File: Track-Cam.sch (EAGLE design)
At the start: 38 parts, among them IC1 STM32F042KT/M, IC2 BD6211F/M, IC3 BD6211F/M, X1 RASPI_BOARD_B+#_HC

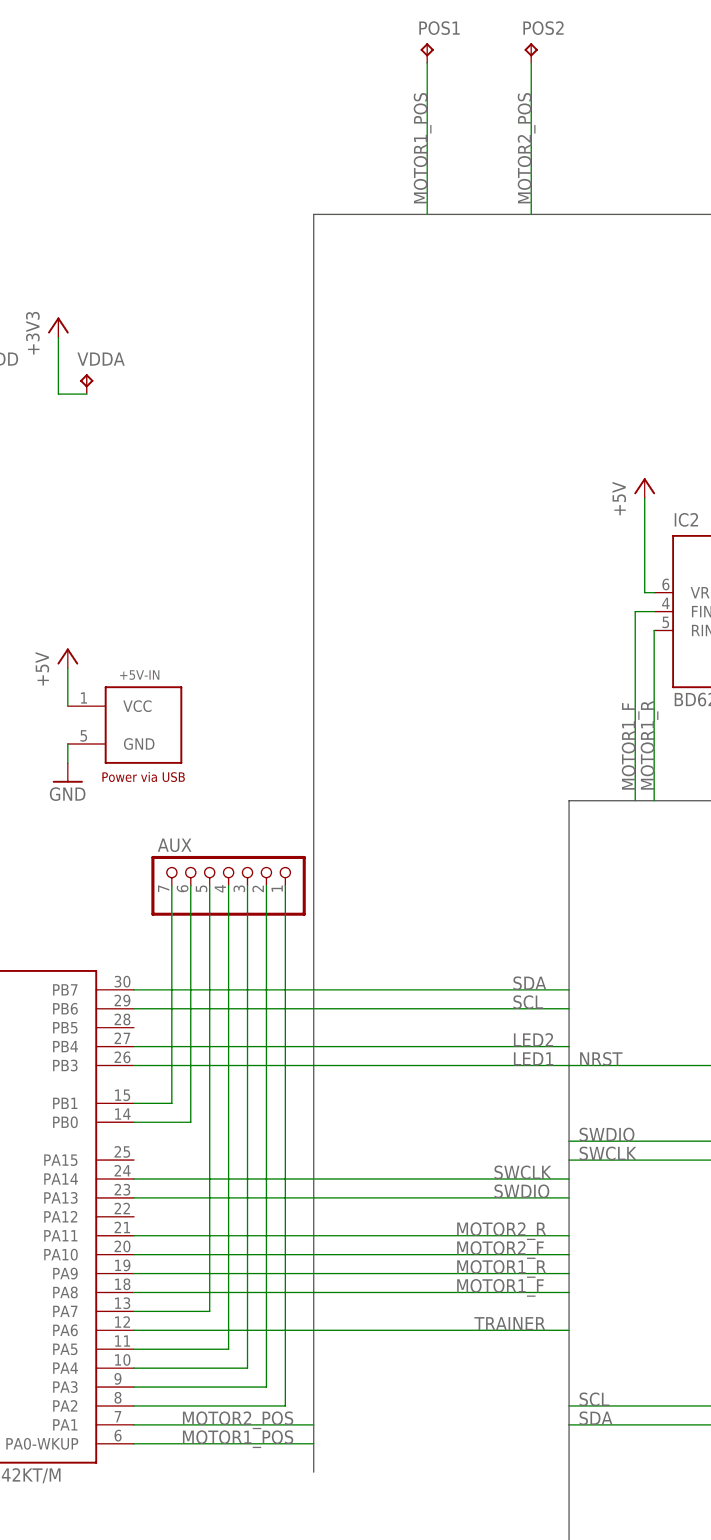
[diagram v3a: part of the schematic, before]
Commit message: replaced components to confirm to actual gimbal size
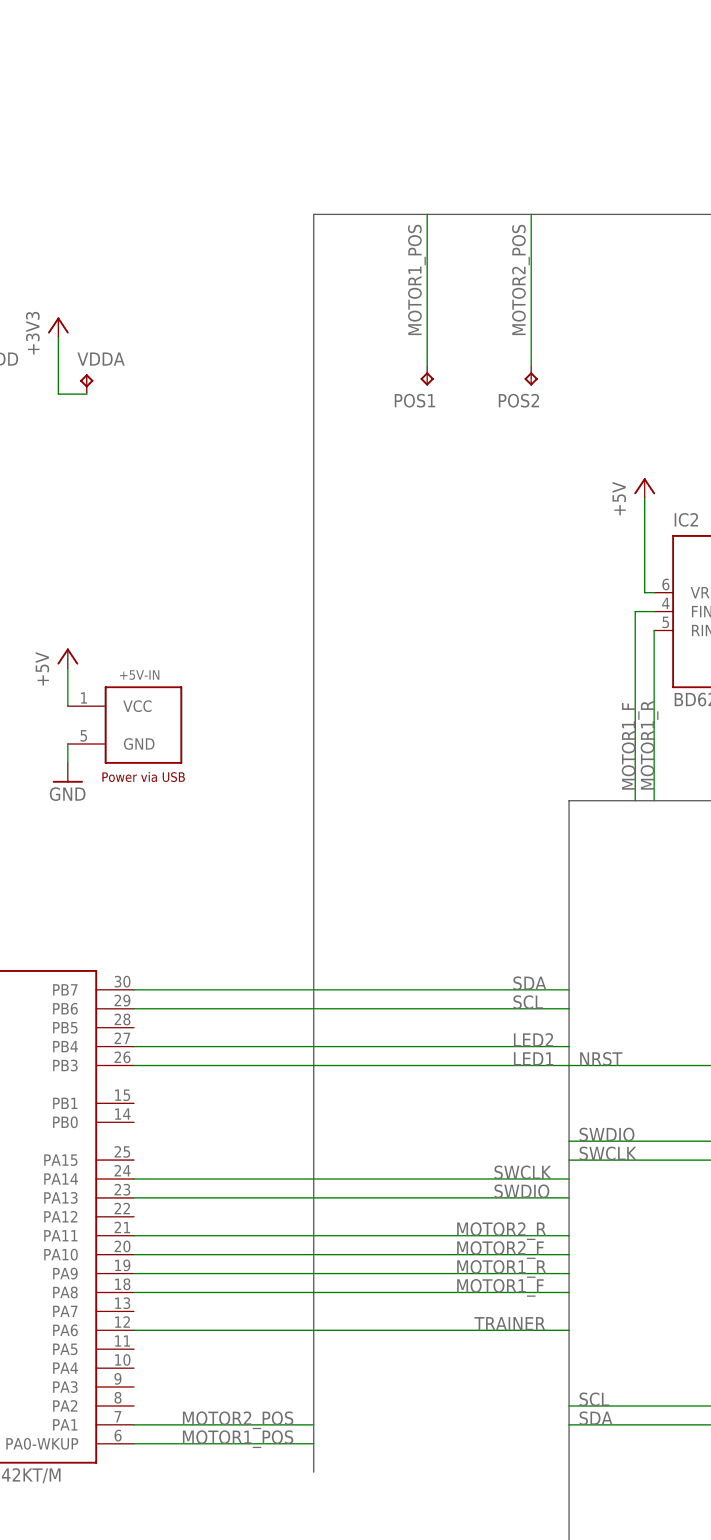
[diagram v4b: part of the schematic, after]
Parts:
- removed AUX: AUX PORT, connector:PINHD-1X7/NS
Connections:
- removed net PA2: AUX.1, IC1MCU.PA2
- removed net PA3: AUX.2, IC1MCU.PA3
- removed net PA4: AUX.3, IC1MCU.PA4
- removed net PA5: AUX.4, IC1MCU.PA5
- removed net PA7: AUX.5, IC1MCU.PA7
- removed net PB0: AUX.6, IC1MCU.PB0
- removed net PB1: AUX.7, IC1MCU.PB1
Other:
- moved on the sheet: POS1, POS2
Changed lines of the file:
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@@
 <part name="2A" library="testpad" deviceset="TP" device="B1,27"/>
 <part name="2B" library="testpad" deviceset="TP" device="B1,27"/>
-<part name="AUX" library="connector" deviceset="PINHD-1X7" device="/NS" value="AUX PORT"/>
 <part name="R5" library="gen-discrete" deviceset="RESISTOR-US" device="2012" value="330"/>
 <part name="LED3" library="gen-discrete" deviceset="LED" device="1608"/>
@@
 <instance part="VDD3" gate="G$1" x="127" y="187.96"/>
 <instance part="+3V5" gate="G$1" x="139.7" y="189.23"/>
-<instance part="POS1" gate="G$1" x="189.23" y="226.06"/>
-<instance part="POS2" gate="G$1" x="203.2" y="226.06"/>
+<instance part="POS1" gate="G$1" x="189.23" y="180.34" rot="R180"/>
+<instance part="POS2" gate="G$1" x="203.2" y="180.34" rot="R180"/>
 <instance part="1A" gate="G$1" x="372.11" y="143.51" rot="R90"/>
 <instance part="1B" gate="G$1" x="379.73" y="143.51" rot="R90"/>
 <instance part="2A" gate="G$1" x="387.35" y="143.51" rot="R90"/>
 <instance part="2B" gate="G$1" x="394.97" y="143.51" rot="R90"/>
-<instance part="AUX" gate="A" x="162.56" y="115.57" smashed="yes" rot="MR90">
-<attribute name="NAME" x="153.035" y="119.38" size="1.778" layer="95" rot="MR180"/>
-</instance>
 <instance part="R5" gate="G$1" x="349.25" y="156.21" rot="R90"/>
 <instance part="LED3" gate="G$1" x="361.95" y="156.21" rot="R90"/>
@@
 <segment>
 <pinref part="POS1" gate="G$1" pin="TP"/>
-<wire x1="189.23" y1="223.52" x2="189.23" y2="203.2" width="0.1524" layer="91"/>
-<label x="189.23" y="204.47" size="1.778" layer="95" rot="R90"/>
+<wire x1="189.23" y1="182.88" x2="189.23" y2="203.2" width="0.1524" layer="91"/>
+<label x="186.69" y="201.93" size="1.778" layer="95" rot="R270"/>
 </segment>
 </net>
@@
 <segment>
 <pinref part="POS2" gate="G$1" pin="TP"/>
-<wire x1="203.2" y1="223.52" x2="203.2" y2="203.2" width="0.1524" layer="91"/>
-<label x="203.2" y="204.47" size="1.778" layer="95" rot="R90"/>
+<wire x1="203.2" y1="182.88" x2="203.2" y2="203.2" width="0.1524" layer="91"/>
+<label x="200.66" y="201.93" size="1.778" layer="95" rot="R270"/>
 </segment>
 </net>
@@
 </segment>
 </net>
-<net name="PA2" class="0">
-<segment>
-<pinref part="IC1" gate="MCU" pin="PA2"/>
-<pinref part="AUX" gate="A" pin="1"/>
-<wire x1="149.86" y1="43.18" x2="170.18" y2="43.18" width="0.1524" layer="91"/>
-<wire x1="170.18" y1="43.18" x2="170.18" y2="113.03" width="0.1524" layer="91"/>
-</segment>
-</net>
-<net name="PA3" class="0">
-<segment>
-<pinref part="IC1" gate="MCU" pin="PA3"/>
-<pinref part="AUX" gate="A" pin="2"/>
-<wire x1="149.86" y1="45.72" x2="167.64" y2="45.72" width="0.1524" layer="91"/>
-<wire x1="167.64" y1="45.72" x2="167.64" y2="113.03" width="0.1524" layer="91"/>
-</segment>
-</net>
-<net name="PA5" class="0">
-<segment>
-<pinref part="IC1" gate="MCU" pin="PA5"/>
-<pinref part="AUX" gate="A" pin="4"/>
-<wire x1="149.86" y1="50.8" x2="162.56" y2="50.8" width="0.1524" layer="91"/>
-<wire x1="162.56" y1="50.8" x2="162.56" y2="113.03" width="0.1524" layer="91"/>
-</segment>
-</net>
-<net name="PA7" class="0">
-<segment>
-<pinref part="IC1" gate="MCU" pin="PA7"/>
-<pinref part="AUX" gate="A" pin="5"/>
-<wire x1="149.86" y1="55.88" x2="160.02" y2="55.88" width="0.1524" layer="91"/>
-<wire x1="160.02" y1="55.88" x2="160.02" y2="113.03" width="0.1524" layer="91"/>
-</segment>
-</net>
-<net name="PB0" class="0">
-<segment>
-<pinref part="IC1" gate="MCU" pin="PB0"/>
-<pinref part="AUX" gate="A" pin="6"/>
-<wire x1="149.86" y1="81.28" x2="157.48" y2="81.28" width="0.1524" layer="91"/>
-<wire x1="157.48" y1="81.28" x2="157.48" y2="113.03" width="0.1524" layer="91"/>
-</segment>
-</net>
-<net name="PB1" class="0">
-<segment>
-<pinref part="IC1" gate="MCU" pin="PB1"/>
-<pinref part="AUX" gate="A" pin="7"/>
-<wire x1="149.86" y1="83.82" x2="154.94" y2="83.82" width="0.1524" layer="91"/>
-<wire x1="154.94" y1="83.82" x2="154.94" y2="113.03" width="0.1524" layer="91"/>
-</segment>
-</net>
-<net name="PA4" class="0">
-<segment>
-<pinref part="IC1" gate="MCU" pin="PA4"/>
-<pinref part="AUX" gate="A" pin="3"/>
-<wire x1="149.86" y1="48.26" x2="165.1" y2="48.26" width="0.1524" layer="91"/>
-<wire x1="165.1" y1="48.26" x2="165.1" y2="113.03" width="0.1524" layer="91"/>
-</segment>
-</net>

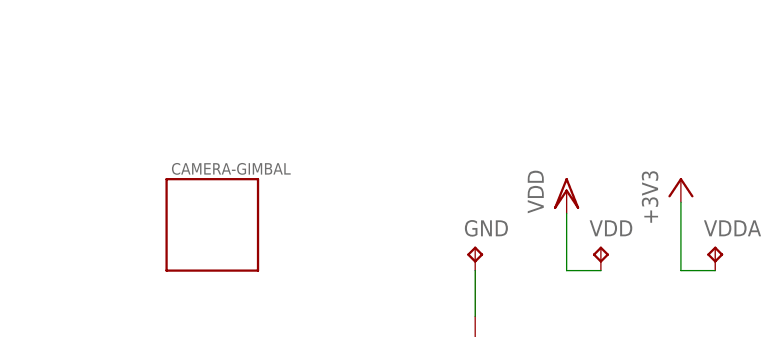
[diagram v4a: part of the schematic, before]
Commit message: improve silk design
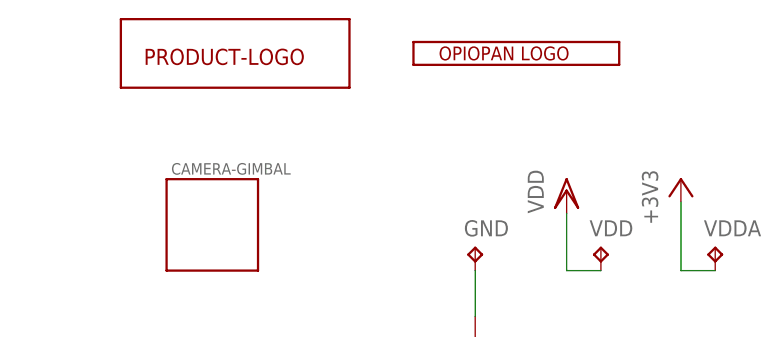
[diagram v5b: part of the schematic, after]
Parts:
- added U$1: PRODUCT-LOGO-TRACKCAM, logo:PRODUCT-LOGO-TRACKCAM
- added U$2: OPIOPAN-LOGO, logo:OPIOPAN-LOGO
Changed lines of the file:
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@@
 <part name="GND15" library="supply1" deviceset="GND" device=""/>
 <part name="XMTR" library="connector" deviceset="53047-0310" device=""/>
+<part name="U$1" library="logo" deviceset="PRODUCT-LOGO" device="-TRACKCAM"/>
+<part name="U$2" library="logo" deviceset="OPIOPAN-LOGO" device=""/>
 </parts>
 <sheets>
@@
 <instance part="GND15" gate="1" x="364.49" y="151.13"/>
 <instance part="XMTR" gate="G$1" x="349.25" y="146.05"/>
+<instance part="U$1" gate="G$1" x="90.17" y="204.47"/>
+<instance part="U$2" gate="G$1" x="120.65" y="203.2"/>
 </instances>
 <busses>

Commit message: fix some bug
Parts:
- C4, C5: value 20p -> 22p; device gen-discrete:CAPACITOR2012 -> gen-discrete:CAPACITOR1608
- R1: value 1M -> 300K; device gen-discrete:RESISTOR-US1608 -> gen-discrete:RESISTOR-US2012
- R2: device generic:RESISTOR-US1608 -> gen-discrete:RESISTOR-US2012
- R3: value 330 -> 300
- R4: value 330 -> 100
- R5: value 330 -> 470
- renumbered X1 to P1
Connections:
- new net N$1: C5.2, R1.1, XT1.2
- net OSC_IN: no longer R1.1
- net OSC_OUT: no longer C5.2, XT1.2
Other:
- moved on the sheet: R1
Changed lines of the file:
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@@
 <parts>
 <part name="IC1" library="stm32" deviceset="STM32F042K*T" device="/M" value="STM32F042KT/M"/>
-<part name="X1" library="raspi" deviceset="RASPI_BOARD_B+#" device="_HC"/>
+<part name="P1" library="raspi" deviceset="RASPI_BOARD_B+#" device="_HC"/>
 <part name="C1" library="gen-discrete" deviceset="CAPACITOR" device="2012" value="0.1μ"/>
 <part name="C2" library="gen-discrete" deviceset="CAPACITOR" device="2012" value="0.1μ"/>
 <part name="C3" library="gen-discrete" deviceset="CAPACITOR" device="2012" value="4.7μ"/>
-<part name="C4" library="gen-discrete" deviceset="CAPACITOR" device="2012" value="20p"/>
-<part name="C5" library="gen-discrete" deviceset="CAPACITOR" device="2012" value="20p"/>
+<part name="C4" library="gen-discrete" deviceset="CAPACITOR" device="1608" value="22p"/>
+<part name="C5" library="gen-discrete" deviceset="CAPACITOR" device="1608" value="22p"/>
 <part name="C6" library="gen-discrete" deviceset="CAPACITOR" device="2012" value="10n"/>
 <part name="C7" library="gen-discrete" deviceset="CAPACITOR" device="2012" value="1μ"/>
 <part name="XT1" library="gen-discrete" deviceset="XTAL/S" device="" value="8MHz"/>
-<part name="R1" library="gen-discrete" deviceset="RESISTOR-US" device="1608" value="1M"/>
-<part name="R2" library="generic" deviceset="RESISTOR-US" device="1608" value="10K"/>
+<part name="R1" library="gen-discrete" deviceset="RESISTOR-US" device="2012" value="300K"/>
+<part name="R2" library="gen-discrete" deviceset="RESISTOR-US" device="2012" value="10K"/>
 <part name="YAW" library="connector" deviceset="53047-0510" device=""/>
 <part name="PITCH" library="connector" deviceset="53047-0510" device=""/>
@@
 <part name="LED1" library="gen-discrete" deviceset="LED" device="1608"/>
 <part name="LED2" library="gen-discrete" deviceset="LED" device="1608"/>
-<part name="R3" library="gen-discrete" deviceset="RESISTOR-US" device="2012" value="330"/>
-<part name="R4" library="gen-discrete" deviceset="RESISTOR-US" device="2012" value="330"/>
+<part name="R3" library="gen-discrete" deviceset="RESISTOR-US" device="2012" value="300"/>
+<part name="R4" library="gen-discrete" deviceset="RESISTOR-US" device="2012" value="100"/>
 <part name="GND14" library="supply1" deviceset="GND" device=""/>
 <part name="GND" library="testpad" deviceset="TP" device="B1,27"/>
@@
 <part name="2A" library="testpad" deviceset="TP" device="B1,27"/>
 <part name="2B" library="testpad" deviceset="TP" device="B1,27"/>
-<part name="R5" library="gen-discrete" deviceset="RESISTOR-US" device="2012" value="330"/>
+<part name="R5" library="gen-discrete" deviceset="RESISTOR-US" device="2012" value="470"/>
 <part name="LED3" library="gen-discrete" deviceset="LED" device="1608"/>
 <part name="GND15" library="supply1" deviceset="GND" device=""/>
@@
 <instances>
 <instance part="IC1" gate="MCU" x="127" y="71.12"/>
-<instance part="X1" gate="G$1" x="251.46" y="76.2"/>
+<instance part="P1" gate="G$1" x="251.46" y="76.2"/>
 <instance part="C1" gate="G$1" x="81.28" y="137.16"/>
 <instance part="C2" gate="G$1" x="92.71" y="137.16"/>
@@
 <instance part="C7" gate="G$1" x="87.63" y="60.96"/>
 <instance part="XT1" gate="G$1" x="85.09" y="91.44" rot="R270"/>
-<instance part="R1" gate="G$1" x="93.98" y="91.44"/>
+<instance part="R1" gate="G$1" x="92.71" y="83.82" rot="R90"/>
 <instance part="R2" gate="G$1" x="101.6" y="33.02"/>
 <instance part="YAW" gate="G$1" x="266.7" y="182.88"/>
@@
 <wire x1="102.87" y1="53.34" x2="102.87" y2="99.06" width="0.1524" layer="91"/>
 <pinref part="C4" gate="G$1" pin="2"/>
-<wire x1="102.87" y1="99.06" x2="93.98" y2="99.06" width="0.1524" layer="91"/>
-<wire x1="93.98" y1="99.06" x2="85.09" y2="99.06" width="0.1524" layer="91"/>
+<wire x1="102.87" y1="99.06" x2="85.09" y2="99.06" width="0.1524" layer="91"/>
 <wire x1="85.09" y1="99.06" x2="76.2" y2="99.06" width="0.1524" layer="91"/>
-<pinref part="R1" gate="G$1" pin="1"/>
-<wire x1="93.98" y1="96.52" x2="93.98" y2="99.06" width="0.1524" layer="91"/>
-<junction x="93.98" y="99.06"/>
 <pinref part="XT1" gate="G$1" pin="1"/>
 <wire x1="85.09" y1="96.52" x2="85.09" y2="99.06" width="0.1524" layer="91"/>
@@
 <net name="OSC_OUT" class="0">
 <segment>
-<pinref part="R1" gate="G$1" pin="2"/>
-<wire x1="93.98" y1="86.36" x2="93.98" y2="83.82" width="0.1524" layer="91"/>
-<wire x1="85.09" y1="83.82" x2="93.98" y2="83.82" width="0.1524" layer="91"/>
-<pinref part="XT1" gate="G$1" pin="2"/>
-<wire x1="85.09" y1="86.36" x2="85.09" y2="83.82" width="0.1524" layer="91"/>
-<junction x="85.09" y="83.82"/>
-<pinref part="C5" gate="G$1" pin="2"/>
-<wire x1="76.2" y1="83.82" x2="85.09" y2="83.82" width="0.1524" layer="91"/>
 <pinref part="IC1" gate="MCU" pin="OSC_OUT"/>
 <wire x1="104.14" y1="50.8" x2="100.33" y2="50.8" width="0.1524" layer="91"/>
 <wire x1="100.33" y1="50.8" x2="100.33" y2="83.82" width="0.1524" layer="91"/>
-<wire x1="100.33" y1="83.82" x2="93.98" y2="83.82" width="0.1524" layer="91"/>
-<junction x="93.98" y="83.82"/>
+<pinref part="R1" gate="G$1" pin="2"/>
+<wire x1="97.79" y1="83.82" x2="100.33" y2="83.82" width="0.1524" layer="91"/>
 </segment>
 </net>
@@
 </segment>
 <segment>
-<pinref part="X1" gate="G$1" pin="3V3B"/>
+<pinref part="P1" gate="G$1" pin="3V3B"/>
 <pinref part="+3V2" gate="G$1" pin="+3V3"/>
 <wire x1="259.08" y1="104.14" x2="266.7" y2="104.14" width="0.1524" layer="91"/>
@@
 </segment>
 <segment>
-<pinref part="X1" gate="G$1" pin="GPIO18"/>
+<pinref part="P1" gate="G$1" pin="GPIO18"/>
 <wire x1="236.22" y1="88.9" x2="208.28" y2="88.9" width="0.1524" layer="91"/>
 <label x="209.55" y="88.9" size="1.778" layer="95"/>
@@
 </segment>
 <segment>
-<pinref part="X1" gate="G$1" pin="GPIO24"/>
+<pinref part="P1" gate="G$1" pin="GPIO24"/>
 <wire x1="236.22" y1="78.74" x2="208.28" y2="78.74" width="0.1524" layer="91"/>
 <label x="209.55" y="78.74" size="1.778" layer="95"/>
@@
 </segment>
 <segment>
-<pinref part="X1" gate="G$1" pin="GPIO25"/>
+<pinref part="P1" gate="G$1" pin="GPIO25"/>
 <wire x1="236.22" y1="76.2" x2="208.28" y2="76.2" width="0.1524" layer="91"/>
 <label x="209.55" y="76.2" size="1.778" layer="95"/>
@@
 </segment>
 <segment>
-<pinref part="X1" gate="G$1" pin="SCL"/>
+<pinref part="P1" gate="G$1" pin="SCL"/>
 <wire x1="236.22" y1="43.18" x2="208.28" y2="43.18" width="0.1524" layer="91"/>
 <label x="209.55" y="43.18" size="1.778" layer="95"/>
@@
 </segment>
 <segment>
-<pinref part="X1" gate="G$1" pin="SDA"/>
+<pinref part="P1" gate="G$1" pin="SDA"/>
 <wire x1="236.22" y1="40.64" x2="208.28" y2="40.64" width="0.1524" layer="91"/>
 <label x="209.55" y="40.64" size="1.778" layer="95"/>
@@
 </segment>
 <segment>
-<pinref part="X1" gate="G$1" pin="3V3A"/>
+<pinref part="P1" gate="G$1" pin="3V3A"/>
 <pinref part="VDD2" gate="G$1" pin="VDD"/>
 <wire x1="256.54" y1="104.14" x2="256.54" y2="110.49" width="0.1524" layer="91"/>
@@
 <net name="GND" class="1">
 <segment>
-<pinref part="X1" gate="G$1" pin="GND_B"/>
+<pinref part="P1" gate="G$1" pin="GND_B"/>
 <wire x1="278.13" y1="66.04" x2="278.13" y2="58.42" width="0.1524" layer="91"/>
 <wire x1="278.13" y1="58.42" x2="278.13" y2="50.8" width="0.1524" layer="91"/>
 <wire x1="266.7" y1="66.04" x2="278.13" y2="66.04" width="0.1524" layer="91"/>
-<pinref part="X1" gate="G$1" pin="GND_E"/>
+<pinref part="P1" gate="G$1" pin="GND_E"/>
 <wire x1="266.7" y1="58.42" x2="278.13" y2="58.42" width="0.1524" layer="91"/>
 <junction x="278.13" y="58.42"/>
-<pinref part="X1" gate="G$1" pin="GND_H"/>
+<pinref part="P1" gate="G$1" pin="GND_H"/>
 <wire x1="266.7" y1="50.8" x2="278.13" y2="50.8" width="0.1524" layer="91"/>
 <pinref part="VSS1" gate="1" pin="GND"/>
@@
 </segment>
 </net>
+<net name="N$1" class="0">
+<segment>
+<pinref part="XT1" gate="G$1" pin="2"/>
+<wire x1="85.09" y1="86.36" x2="85.09" y2="83.82" width="0.1524" layer="91"/>
+<pinref part="C5" gate="G$1" pin="2"/>
+<wire x1="76.2" y1="83.82" x2="85.09" y2="83.82" width="0.1524" layer="91"/>
+<pinref part="R1" gate="G$1" pin="1"/>
+<wire x1="87.63" y1="83.82" x2="85.09" y2="83.82" width="0.1524" layer="91"/>
+<junction x="85.09" y="83.82"/>
+</segment>
+</net>
